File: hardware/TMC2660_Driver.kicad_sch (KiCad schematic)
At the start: 30 parts, among them J1 PCIe_Stepper, J2 Conn_01x04_Male, U1 TMC2660, U2 74LVC1G06, U3 24LC02

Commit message: Update 2660 and 2130 driver fab files.
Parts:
- FID1, FID2, FID3, FID4, H1, H2, LOGO1: now left out of the parts list

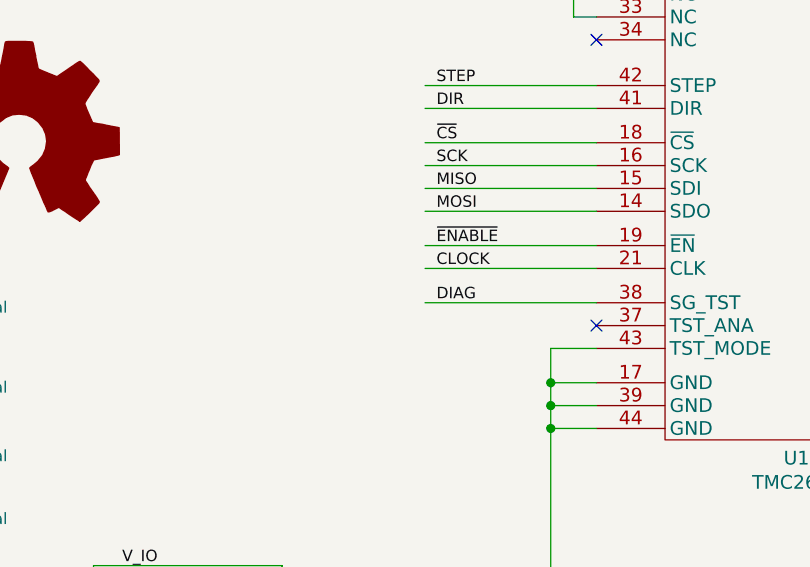
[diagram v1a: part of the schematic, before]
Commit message: Convert SCH files to latest version. Fix DRC Warnings in PrntrBoard.
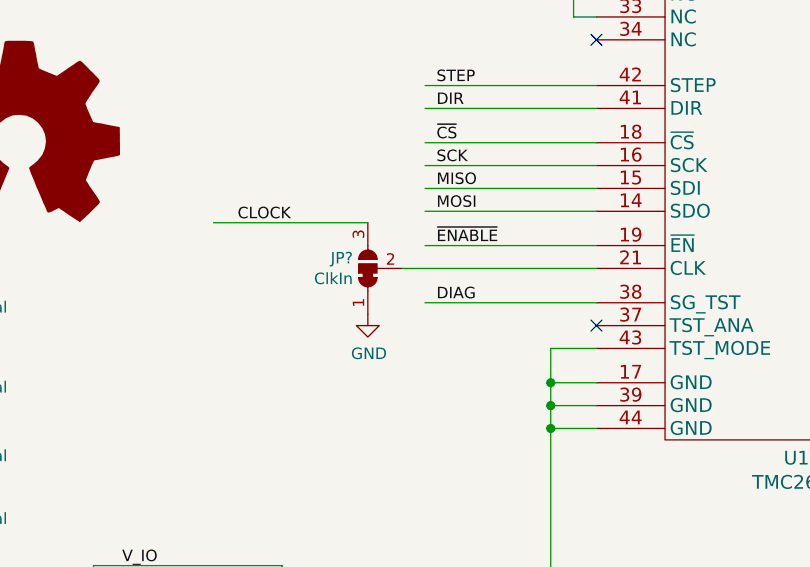
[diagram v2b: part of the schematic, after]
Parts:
- added JP?: ClkIn, Jumper:SolderJumper-3_P1.3mm_Bridged12_Pad1.0x1.5mm, symbol Jumper:SolderJumper_3_Bridged12
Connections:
- net CLOCK: now also JP?.3 (B); no longer U1.21 (CLK)
- net GND: now also JP?.1 (A)
- net ~CS renamed ~{CS}
- net ~ENABLE renamed ~{ENABLE}
- net ~RESET renamed ~{RESET}
- net ~SLEEP renamed ~{SLEEP}
- new net: JP?.2 (C), U1.21 (CLK)

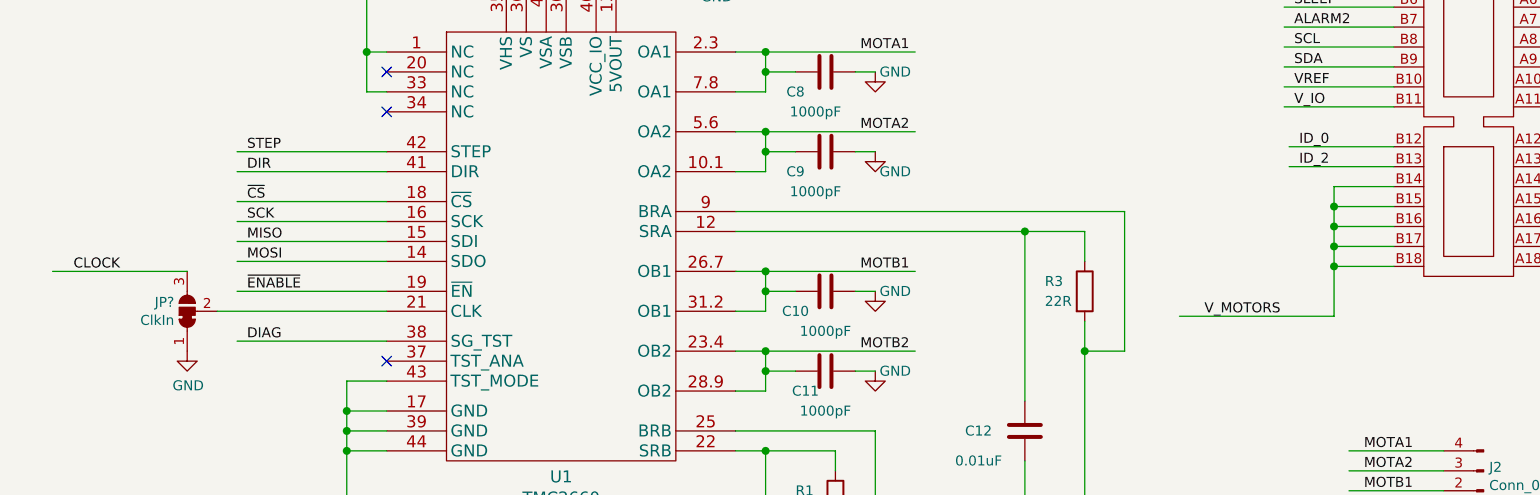
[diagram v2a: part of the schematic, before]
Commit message: Update drivers to respect high motor coltage circuit.
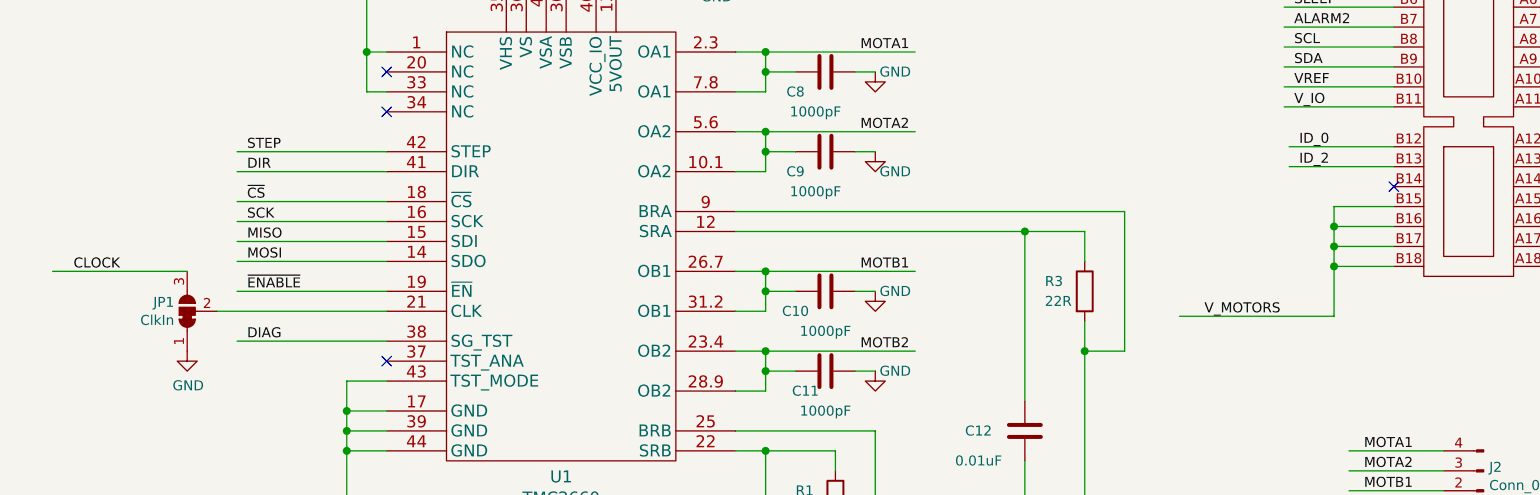
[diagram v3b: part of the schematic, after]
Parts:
- gave numbers to parts that had none: 1
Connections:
- net V_MOTORS: no longer J1.B14
- no-connect marks 3 -> 4
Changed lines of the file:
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@@
   (junction (at 182.88 152.4) (diameter 1.016) (color 0 0 0 0))
   (junction (at 190.5 105.41) (diameter 1.016) (color 0 0 0 0))
-  (junction (at 222.25 86.995) (diameter 1.016) (color 0 0 0 0))
   (junction (at 222.25 89.535) (diameter 1.016) (color 0 0 0 0))
   (junction (at 222.25 92.075) (diameter 1.016) (color 0 0 0 0))
@@
   (no_connect (at 101.6 74.93))
   (no_connect (at 101.6 106.68))
+  (no_connect (at 229.87 84.455))
   (wire (pts (xy 27.94 146.05) (xy 38.1 146.05))
     (stroke (width 0) (type solid) (color 0 0 0 0))
@@
     (stroke (width 0) (type solid) (color 0 0 0 0))
   )
-  (wire (pts (xy 222.25 84.455) (xy 222.25 86.995))
-    (stroke (width 0) (type solid) (color 0 0 0 0))
-  )
   (wire (pts (xy 222.25 86.995) (xy 222.25 89.535))
     (stroke (width 0) (type solid) (color 0 0 0 0))
@@
   )
   (wire (pts (xy 229.87 81.915) (xy 216.535 81.915))
-    (stroke (width 0) (type solid) (color 0 0 0 0))
-  )
-  (wire (pts (xy 229.87 84.455) (xy 222.25 84.455))
     (stroke (width 0) (type solid) (color 0 0 0 0))
   )
@@
   (symbol (lib_id "power:GND") (at 76.2 105.41 0) (unit 1)
     (in_bom yes) (on_board yes)
-    (property "Reference" "#PWR?" (id 0) (at 76.2 111.76 0)
+    (property "Reference" "#PWR0102" (id 0) (at 76.2 111.76 0)
       (effects (font (size 1.27 1.27)) hide)
     )
@@
   (symbol (lib_id "Jumper:SolderJumper_3_Bridged12") (at 76.2 100.33 90) (unit 1)
     (in_bom no) (on_board yes)
-    (property "Reference" "JP?" (id 0) (at 74.549 99.1806 90)
+    (property "Reference" "JP1" (id 0) (at 74.549 99.1806 90)
       (effects (font (size 1.27 1.27)) (justify left))
     )
@@
     )
     (path "/3547259f-f383-4845-821f-c157216ba8f8"
-      (reference "#PWR?") (unit 1) (value "GND") (footprint "")
+      (reference "#PWR0102") (unit 1) (value "GND") (footprint "")
     )
     (path "/00000000-0000-0000-0000-00005aca36b2"
@@
     )
     (path "/baaa715a-047f-4de8-86b2-3015cdcef22f"
-      (reference "JP?") (unit 1) (value "ClkIn") (footprint "Jumper:SolderJumper-3_P1.3mm_Bridged12_Pad1.0x1.5mm")
+      (reference "JP1") (unit 1) (value "ClkIn") (footprint "Jumper:SolderJumper-3_P1.3mm_Bridged12_Pad1.0x1.5mm")
     )
     (path "/00000000-0000-0000-0000-00005d9582b1"
